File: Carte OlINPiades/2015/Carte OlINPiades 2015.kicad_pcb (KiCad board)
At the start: 2 copper layers, 283 parts, among them U1 dsPIC33FJ128MC802, U2 LM7805, U3 LM2937-3.3

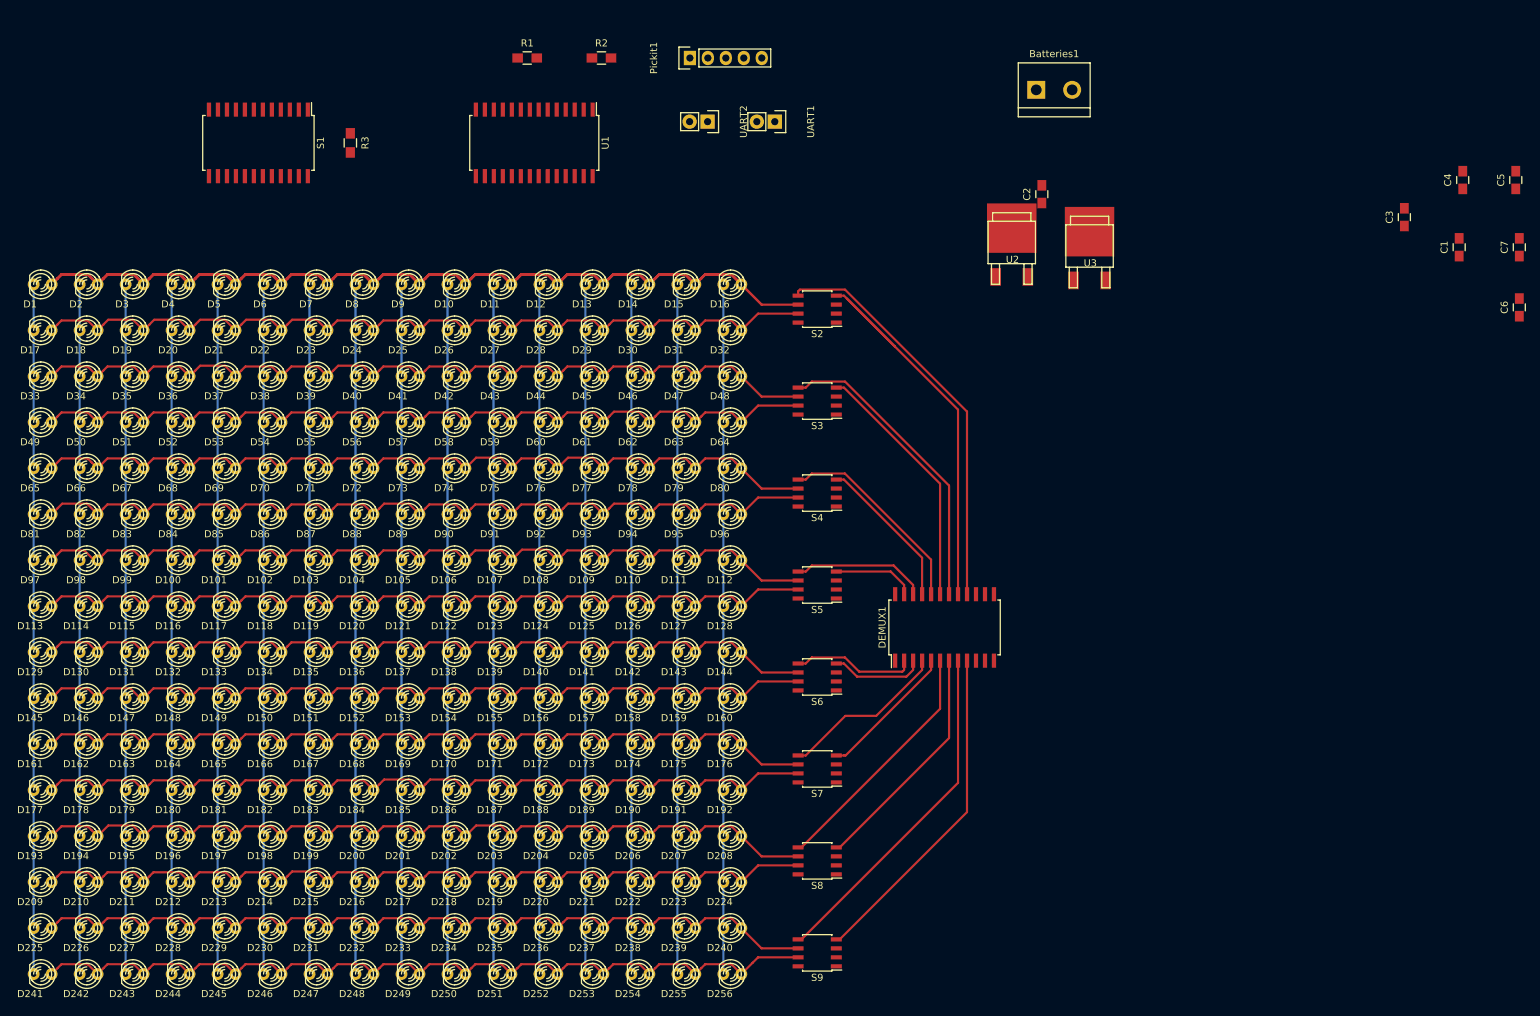
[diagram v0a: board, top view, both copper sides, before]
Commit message: ajoute piste du driver vers leds
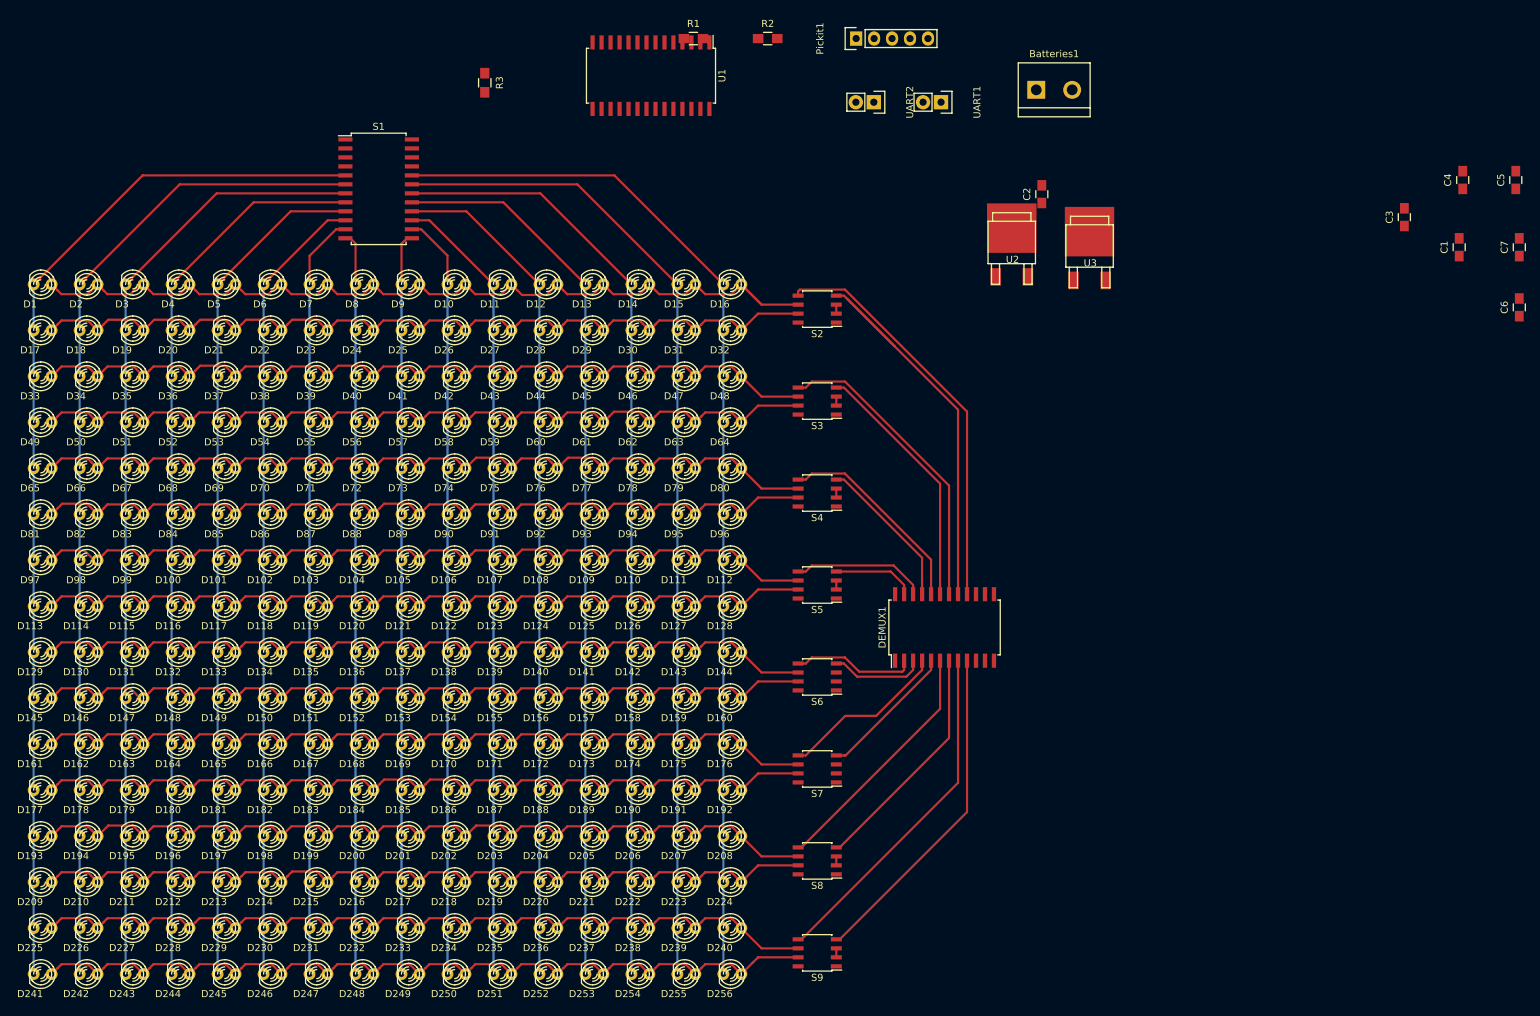
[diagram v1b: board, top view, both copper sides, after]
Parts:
- moved Pickit1 23.7 mm to (162.5, 29.2)
- moved R1 23.7 mm to (139.5, 29.2)
- moved R2 23.7 mm to (150.0, 29.2)
- moved UART1 23.7 mm to (174.5, 38.2)
- moved UART2 23.7 mm to (165.0, 38.2)
- moved R3 20.8 mm to (110.0, 35.5)
- moved U1 19.0 mm to (133.5, 34.5)
- moved S1 18.2 mm to (95.0, 50.5), turned to 0 degrees
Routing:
- net Net-(D1-Pad1): track 472.5 -> 128.2 mm
- net Net-(D1-Pad2): track 97.5 -> 148.0 mm
- net Net-(D112-Pad2): track 97.5 -> 147.9 mm
- net Net-(D114-Pad2): track 97.5 -> 140.9 mm
- net Net-(D111-Pad2): track 97.5 -> 140.9 mm
- net Net-(D115-Pad2): track 97.5 -> 133.9 mm
- net Net-(D110-Pad2): track 97.5 -> 133.9 mm
- net Net-(D100-Pad2): track 97.5 -> 126.9 mm
- net Net-(D109-Pad2): track 97.5 -> 126.8 mm
- net Net-(D101-Pad2): track 97.5 -> 119.8 mm
- net Net-(D108-Pad2): track 97.5 -> 119.8 mm
- net Net-(D102-Pad2): track 97.5 -> 112.8 mm
- net Net-(D107-Pad2): track 97.5 -> 112.8 mm
- net Net-(D103-Pad2): track 97.5 -> 108.2 mm
- net Net-(D10-Pad2): track 97.5 -> 108.1 mm
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
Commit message: alim coté démux
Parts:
- moved R3 15.7 mm to (95.0, 40.0), turned to 0 degrees
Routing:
- net GND: track 0.00 -> 165.4 mm, vias 0 -> 8
- net +5V: track 7.62 -> 141.6 mm, vias 0 -> 8
- net Net-(R3-Pad2): track 0.00 -> 6.94 mm

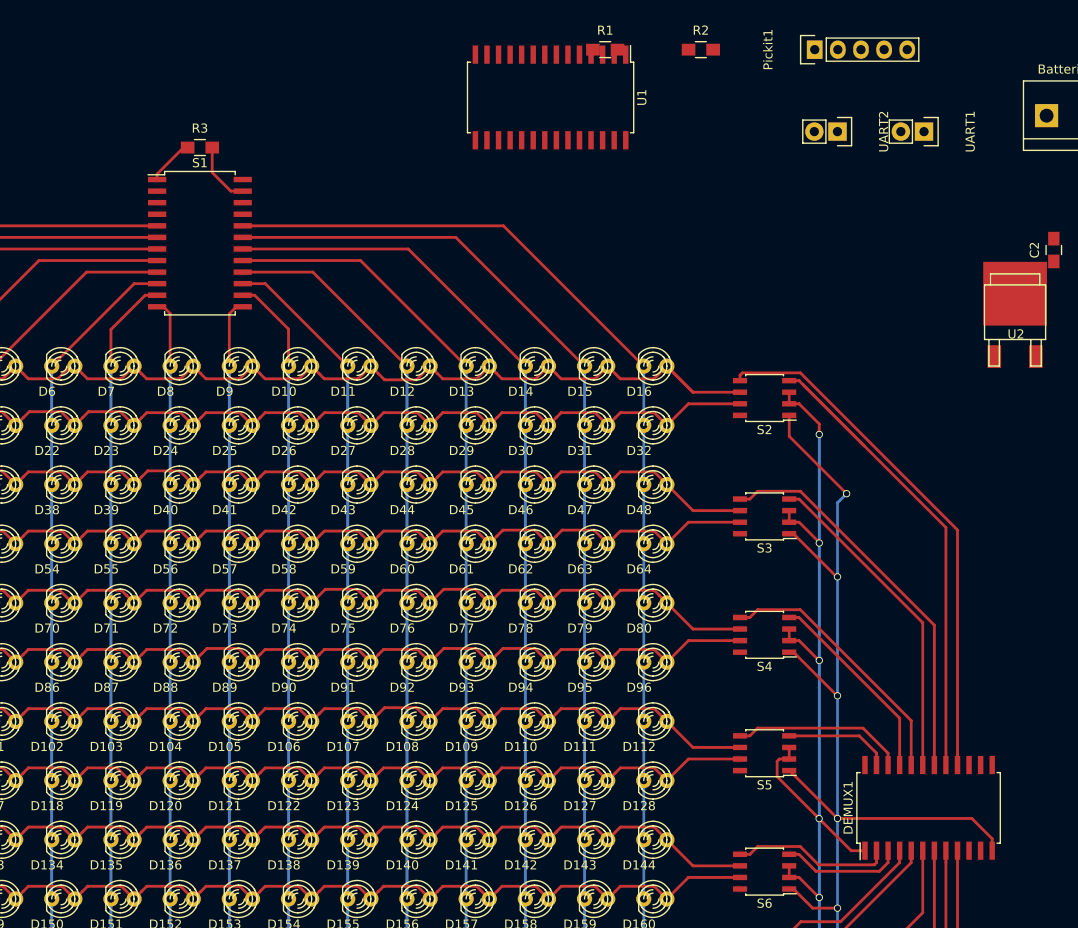
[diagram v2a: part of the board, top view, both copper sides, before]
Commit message: ajoute les pistes de signals
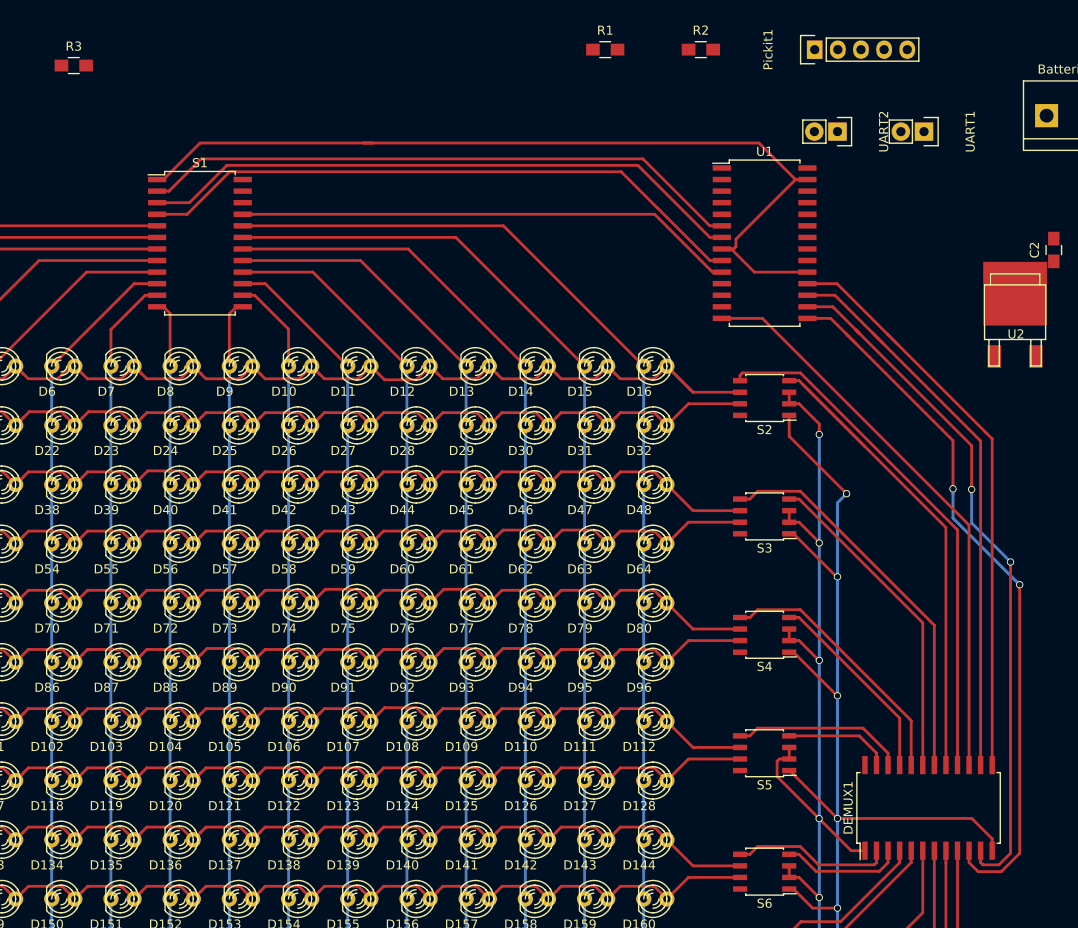
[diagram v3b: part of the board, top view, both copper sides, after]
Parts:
- moved U1 28.4 mm to (157.0, 50.5), turned to 0 degrees
- moved R3 16.5 mm to (81.2, 31.0)
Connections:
- DEMUX1 pad 15: RB10 -> RB5
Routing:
- net GND: track 165.4 -> 258.2 mm
- net RB6: track 0.00 -> 79.3 mm, vias 0 -> 2
- net RB7: track 0.00 -> 76.7 mm, vias 0 -> 2
- net RA2: track 0.00 -> 68.0 mm
- net RB3: track 0.00 -> 67.0 mm
- net RB2: track 0.00 -> 66.5 mm
- net RB9: track 0.00 -> 64.6 mm
- net RB5: track 0.00 -> 62.9 mm
- net RB8: track 0.00 -> 62.9 mm
- net RA3: track 0.00 -> 55.2 mm
- net Net-(R3-Pad2): track 6.94 -> 0.00 mm

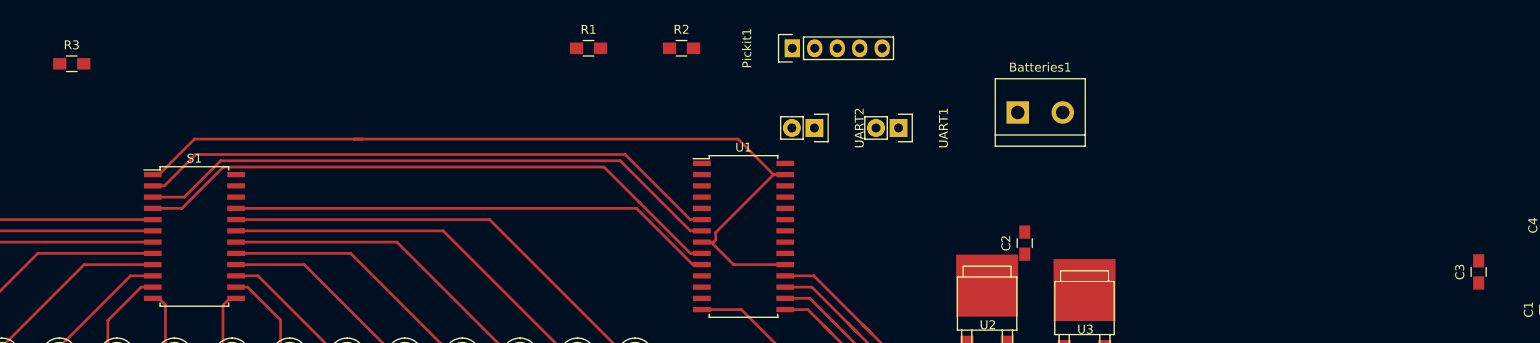
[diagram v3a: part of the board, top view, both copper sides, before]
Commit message: ajoute la partie pour flasher le pic
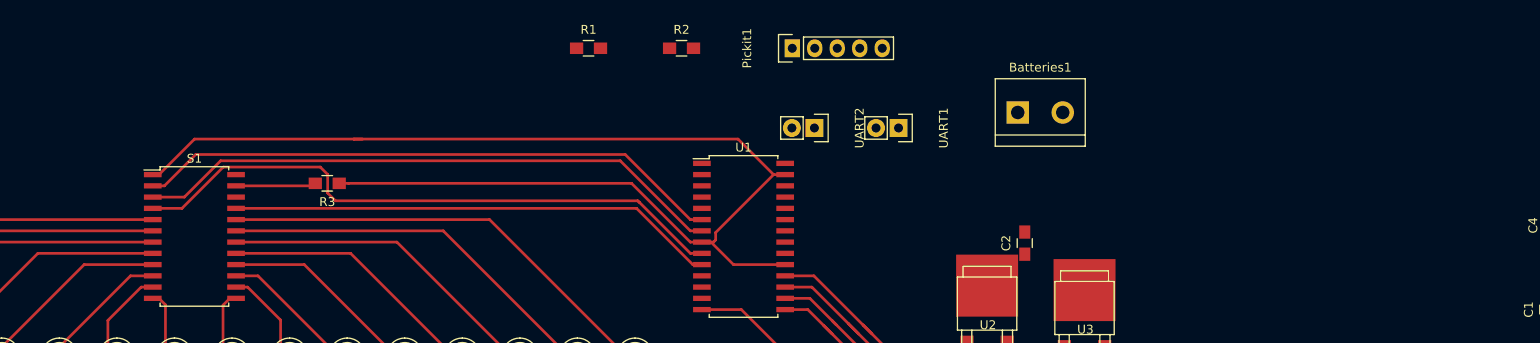
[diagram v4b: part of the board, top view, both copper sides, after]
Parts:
- removed C3: 15pF, Capacitors_SMD:C_0805_HandSoldering
- moved R3 31.9 mm to (110.0, 44.5), turned to 180 degrees
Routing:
- net GND: track 258.2 -> 301.9 mm
- net Net-(R3-Pad2): track 0.00 -> 9.07 mm
- net RA2: track 68.0 -> 69.2 mm
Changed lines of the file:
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@@
     (thickness 1.6)
     (drawings 0)
-    (tracks 1294)
+    (tracks 1304)
     (zones 0)
-    (modules 283)
+    (modules 282)
     (nets 87)
   )
@@
   )
   (module Capacitors_SMD:C_0805_HandSoldering (layer F.Cu)
-    (at 240 54.5 90)
-    (descr "Capacitor SMD 0805, hand soldering")
-    (tags "capacitor 0805")
-    (attr smd)
-    (fp_text reference C3 (at 0 -2.1 90) (layer F.SilkS)
-      (effects (font (size 1 1) (thickness 0.15)))
-    )
-    (fp_text value 15pF (at 0 2.1 90) (layer F.Fab)
-      (effects (font (size 1 1) (thickness 0.15)))
-    )
-    (fp_line (start -2.3 -1) (end 2.3 -1) (layer F.CrtYd) (width 0.05))
-    (fp_line (start -2.3 1) (end 2.3 1) (layer F.CrtYd) (width 0.05))
-    (fp_line (start -2.3 -1) (end -2.3 1) (layer F.CrtYd) (width 0.05))
-    (fp_line (start 2.3 -1) (end 2.3 1) (layer F.CrtYd) (width 0.05))
-    (fp_line (start 0.5 -0.85) (end -0.5 -0.85) (layer F.SilkS) (width 0.15))
-    (fp_line (start -0.5 0.85) (end 0.5 0.85) (layer F.SilkS) (width 0.15))
-    (pad 1 smd rect (at -1.25 0 90) (size 1.5 1.25) (layers F.Cu F.Paste F.Mask)
-      (net 2 GND))
-    (pad 2 smd rect (at 1.25 0 90) (size 1.5 1.25) (layers F.Cu F.Paste F.Mask)
-      (net 5 "Net-(C3-Pad2)"))
-    (model Capacitors_SMD.3dshapes/C_0805_HandSoldering.wrl
-      (at (xyz 0 0 0))
-      (scale (xyz 1 1 1))
-      (rotate (xyz 0 0 0))
-    )
-  )
-  (module Capacitors_SMD:C_0805_HandSoldering (layer F.Cu)
     (at 248.25 49.25 90)
     (descr "Capacitor SMD 0805, hand soldering")
@@
   )
   (module Resistors_SMD:R_0805_HandSoldering (layer F.Cu)
-    (at 81.15 31)
+    (at 110 44.5 180)
     (descr "Resistor SMD 0805, hand soldering")
     (tags "resistor 0805")
     (attr smd)
-    (fp_text reference R3 (at 0 -2.1) (layer F.SilkS)
+    (fp_text reference R3 (at 0 -2.1 180) (layer F.SilkS)
       (effects (font (size 1 1) (thickness 0.15)))
     )
-    (fp_text value TODO (at 0 2.1) (layer F.Fab)
+    (fp_text value TODO (at 0 2.1 180) (layer F.Fab)
       (effects (font (size 1 1) (thickness 0.15)))
     )
@@
     (fp_line (start 0.6 0.875) (end -0.6 0.875) (layer F.SilkS) (width 0.15))
     (fp_line (start -0.6 -0.875) (end 0.6 -0.875) (layer F.SilkS) (width 0.15))
-    (pad 1 smd rect (at -1.35 0) (size 1.5 1.3) (layers F.Cu F.Paste F.Mask)
+    (pad 1 smd rect (at -1.35 0 180) (size 1.5 1.3) (layers F.Cu F.Paste F.Mask)
       (net 2 GND))
-    (pad 2 smd rect (at 1.35 0) (size 1.5 1.3) (layers F.Cu F.Paste F.Mask)
+    (pad 2 smd rect (at 1.35 0 180) (size 1.5 1.3) (layers F.Cu F.Paste F.Mask)
       (net 62 "Net-(R3-Pad2)"))
     (model Resistors_SMD.3dshapes/R_0805_HandSoldering.wrl
@@
     )
   )
+  (segment (start 152.3 51.135) (end 150.992 51.135) (width 0.308) (layer F.Cu) (net 2))
+  (segment (start 150.992 51.135) (end 144.357 44.5) (width 0.308) (layer F.Cu) (net 2))
+  (segment (start 144.357 44.5) (end 112.408 44.5) (width 0.308) (layer F.Cu) (net 2))
+  (segment (start 112.408 44.5) (end 111.35 44.5) (width 0.308) (layer F.Cu) (net 2))
   (segment (start 113 39.5) (end 114 39.5) (width 0.308) (layer F.Cu) (net 2))
   (segment (start 95.015 39.5) (end 113 39.5) (width 0.308) (layer F.Cu) (net 2))
@@
   (segment (start 167.388 104.595) (end 169.285 106.492) (width 0.308) (layer F.Cu) (net 58))
   (segment (start 169.285 106.492) (end 169.285 107.8) (width 0.308) (layer F.Cu) (net 58))
+  (segment (start 99.7 44.785) (end 108.365 44.785) (width 0.308) (layer F.Cu) (net 62))
+  (segment (start 108.365 44.785) (end 108.65 44.5) (width 0.308) (layer F.Cu) (net 62))
   (segment (start 90.3 44.785) (end 91.608 44.785) (width 0.308) (layer F.Cu) (net 63))
   (segment (start 91.608 44.785) (end 95.148021 41.244979) (width 0.308) (layer F.Cu) (net 63))
@@
   (segment (start 143.079989 41.952989) (end 97.963532 41.952989) (width 0.308) (layer F.Cu) (net 64))
   (segment (start 97.963532 41.952989) (end 93.861522 46.055) (width 0.308) (layer F.Cu) (net 64))
-  (segment (start 151.004076 52.405) (end 152.3 52.405) (width 0.308) (layer F.Cu) (net 65))
-  (segment (start 145.216066 46.61699) (end 151.004076 52.405) (width 0.308) (layer F.Cu) (net 65))
-  (segment (start 141.247999 42.660999) (end 145.203989 46.616989) (width 0.308) (layer F.Cu) (net 65))
-  (segment (start 98.256799 42.660999) (end 141.247999 42.660999) (width 0.308) (layer F.Cu) (net 65))
   (segment (start 90.3 47.325) (end 93.592798 47.325) (width 0.308) (layer F.Cu) (net 65))
+  (segment (start 110.923549 46.470751) (end 145.057751 46.470751) (width 0.308) (layer F.Cu) (net 65))
   (segment (start 93.592798 47.325) (end 98.256799 42.660999) (width 0.308) (layer F.Cu) (net 65))
+  (segment (start 98.256799 42.660999) (end 109.208201 42.660999) (width 0.308) (layer F.Cu) (net 65))
+  (segment (start 109.208201 42.660999) (end 110.045999 43.498797) (width 0.308) (layer F.Cu) (net 65))
+  (segment (start 110.045999 43.498797) (end 110.045999 45.593201) (width 0.308) (layer F.Cu) (net 65))
+  (segment (start 110.045999 45.593201) (end 110.923549 46.470751) (width 0.308) (layer F.Cu) (net 65))
+  (segment (start 145.057751 46.470751) (end 145.203989 46.616989) (width 0.308) (layer F.Cu) (net 65))
   (segment (start 145.203989 46.616989) (end 145.216066 46.61699) (width 0.308) (layer F.Cu) (net 65))
+  (segment (start 145.216066 46.61699) (end 151.004076 52.405) (width 0.308) (layer F.Cu) (net 65))
+  (segment (start 151.004076 52.405) (end 152.3 52.405) (width 0.308) (layer F.Cu) (net 65))
   (segment (start 144.922798 47.325) (end 151.272798 53.675) (width 0.308) (layer F.Cu) (net 66))
   (segment (start 99.7 47.325) (end 144.922798 47.325) (width 0.308) (layer F.Cu) (net 66))
